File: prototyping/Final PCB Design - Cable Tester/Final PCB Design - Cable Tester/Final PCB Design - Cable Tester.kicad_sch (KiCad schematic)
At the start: 42 parts, among them J1 Massimo Connector, J2 Banana Jack, J3 Barrel Jack, J4 Conn_01x28_Socket, J5 Conn_01x28_Socket, J6 Touchscreen HMI, J7 Debug Connections, J8 SD Card Reader, J9 2908-05WB-MG, SW1 Rocker Switch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

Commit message: Update traces.
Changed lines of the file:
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@@
 (kicad_sch
-	(version 20231120)
+	(version 20250114)
 	(generator "eeschema")
-	(generator_version "8.0")
+	(generator_version "9.0")
 	(paper "A4")
+	(rectangle
+		(start 19.05 17.145)
+		(end 161.925 52.705)
+		(stroke
+			(width 0)
+			(type default)
+		)
+		(fill
+			(type none)
+		)
+	)
+	(text "Power"
+		(exclude_from_sim no)
+		(at 65.024 22.606 0)
+		(effects
+			(font
+				(size 2.032 2.032)
+				(thickness 0.4064)
+				(bold yes)
+			)
+		)
+	)
+	(text "Signal Relay"
+		(exclude_from_sim no)
+		(at 209.296 48.514 0)
+		(effects
+			(font
+				(size 2.032 2.032)
+				(thickness 0.4064)
+				(bold yes)
+			)
+		)
+	)
+	(text "AVR128DB48\nMicrocontroller"
+		(exclude_from_sim no)
+		(at 92.456 64.77 0)
+		(effects
+			(font
+				(size 2.54 2.54)
+				(thickness 0.508)
+				(bold yes)
+			)
+		)
+	)
+	(text "Analog IF"
+		(exclude_from_sim no)
+		(at 240.284 59.436 0)
+		(effects
+			(font
+				(size 2.032 2.032)
+				(thickness 0.4064)
+				(bold yes)
+			)
+		)
+	)
 	(junction
 		(at 269.24 110.49)
@@
 		)
 	)
-	(rectangle
-		(start 19.05 17.145)
-		(end 161.925 52.705)
-		(stroke
-			(width 0)
-			(type default)
-		)
-		(fill
-			(type none)
-		)
-	)
-	(text "Power"
-		(exclude_from_sim no)
-		(at 65.024 22.606 0)
-		(effects
-			(font
-				(size 2.032 2.032)
-				(thickness 0.4064)
-				(bold yes)
-			)
-		)
-	)
-	(text "Signal Relay"
-		(exclude_from_sim no)
-		(at 209.296 48.514 0)
-		(effects
-			(font
-				(size 2.032 2.032)
-				(thickness 0.4064)
-				(bold yes)
-			)
-		)
-	)
-	(text "AVR128DB48\nMicrocontroller"
-		(exclude_from_sim no)
-		(at 92.456 64.77 0)
-		(effects
-			(font
-				(size 2.54 2.54)
-				(thickness 0.508)
-				(bold yes)
-			)
-		)
-	)
-	(text "Analog IF"
-		(exclude_from_sim no)
-		(at 240.284 59.436 0)
-		(effects
-			(font
-				(size 2.032 2.032)
-				(thickness 0.4064)
-				(bold yes)
-			)
-		)
-	)
 	(label "9V"
 		(at 39.37 33.02 0)
@@
 		)
 	)
+	(embedded_fonts no)
 )

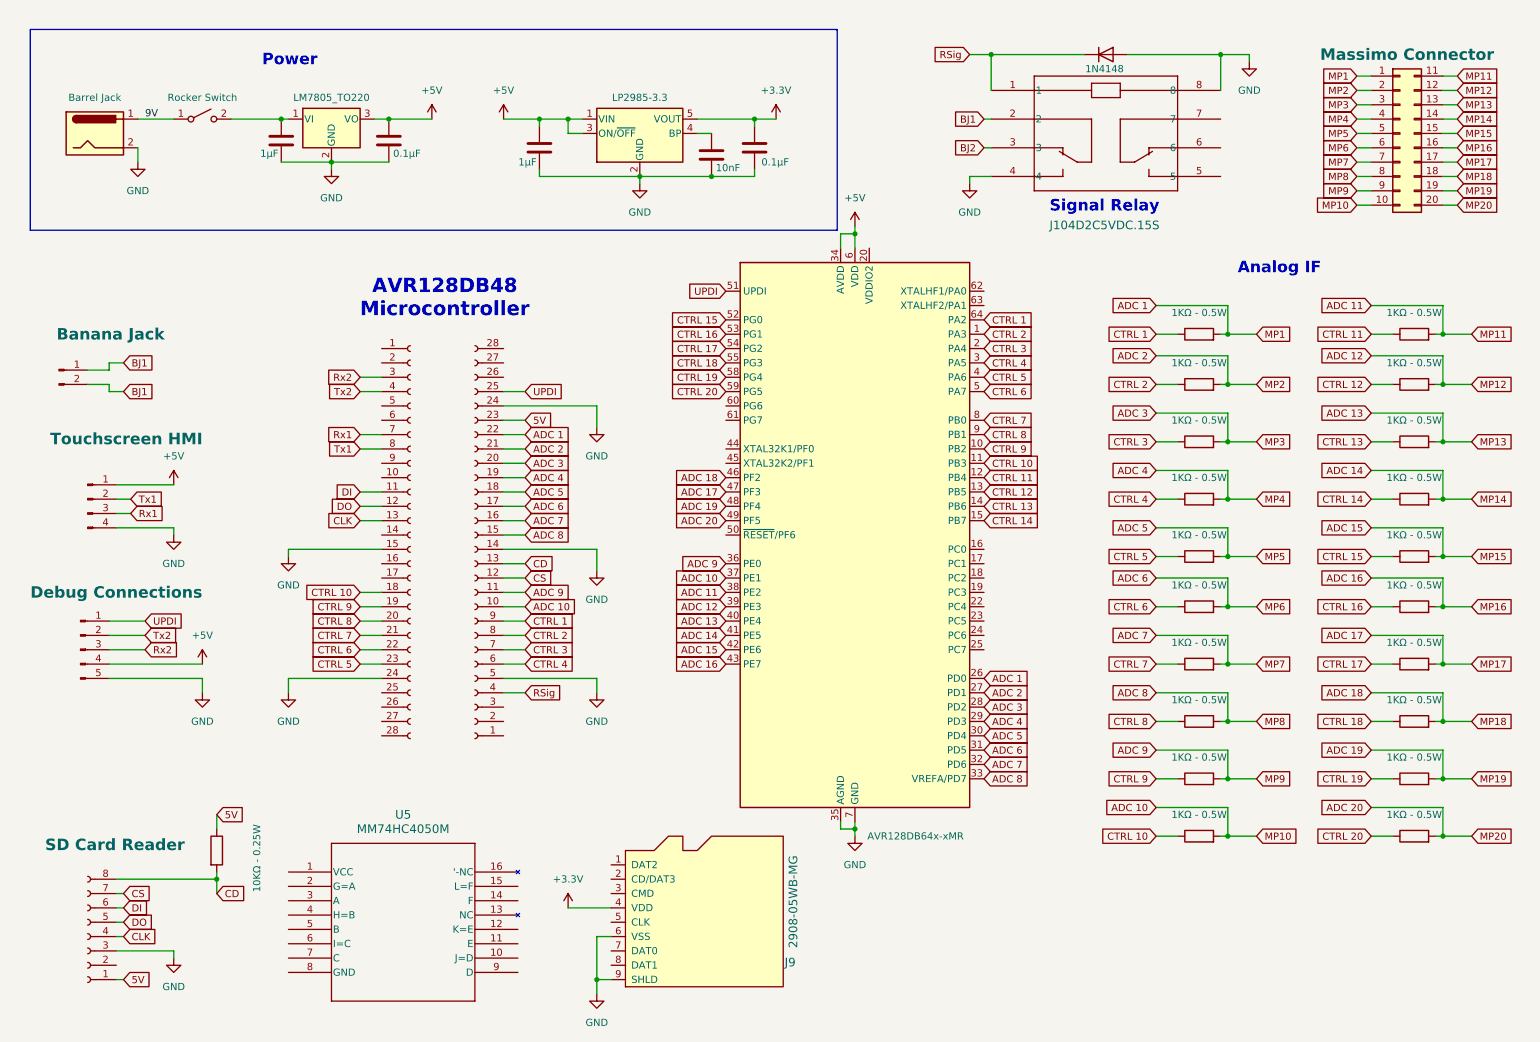
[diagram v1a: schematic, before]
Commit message: Final PCB Schematic updates
updated the pinout for the 64pin MCU, added the FT232RL for rs232 translation, added a micro USB to be the debug connection, added a single pin for UPDI connection.
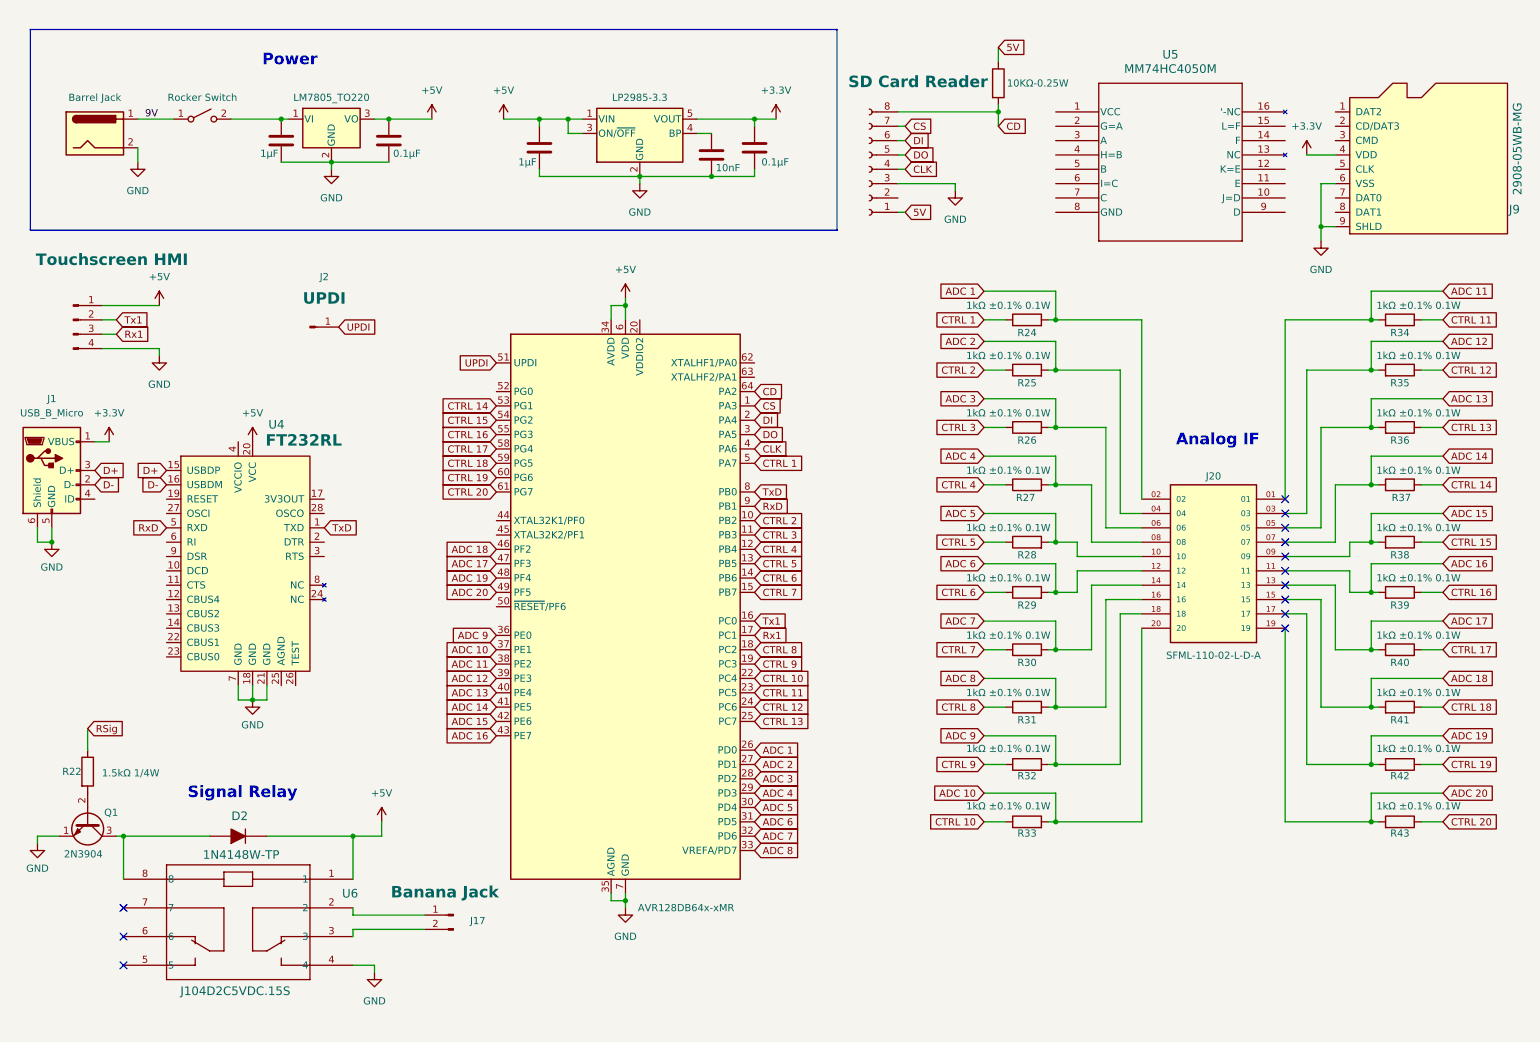
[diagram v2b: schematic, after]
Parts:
- removed D1: 1N4148, Diode_THT:D_DO-35_SOD27_P7.62mm_Horizontal, symbol Diode:1N4148
- removed J1: Massimo Connector, symbol Connector_Generic:Conn_02x10_Top_Bottom
- removed J2: Banana Jack, symbol Connector:Conn_01x02_Pin
- removed J4, J5: Conn_01x28_Socket, symbol Connector:Conn_01x28_Socket
- removed J7: Debug Connections, symbol Connector:Conn_01x05_Pin
- removed R10, R11, R12, R13, R14, R15, R16, R17, R18, R19, R2, R20, R21, R3, R4, R5, R6, R7, R8, R9: 1KΩ - 0.5W, symbol Device:R
- removed U4: J104D2C5VDC.15S, RELAY8_J104D2C5VDC.20S_CRS, symbol 2025-01-29_01-04-30:J104D2C5VDC.20S
- added D2: 1N4148W-TP, digikey-footprints:SOD-123, symbol dk_Diodes-Rectifiers-Single:1N4148W-TP
- added J1: USB_B_Micro, symbol Connector:USB_B_Micro
- added J17: Banana Jack, Connector_PinHeader_2.54mm:PinHeader_1x02_P2.54mm_Vertical, symbol Connector:Conn_01x02_Pin
- added J2: UPDI, Connector_PinHeader_1.00mm:PinHeader_1x01_P1.00mm_Vertical, symbol Connector:Conn_01x01_Pin
- added J20: SFML-110-02-L-D-A, KiCad Symbols and Footprints:SAMTEC_SFML-110-02-L-D-A, symbol SFML-110-02-L-D-A:SFML-110-02-L-D-A
- added Q1: 2N3904, Package_TO_SOT_THT:TO-92_Inline, symbol Transistor_BJT:2N3904
- added R22: 1.5kΩ 1/4W, KiCad Symbols and Footprints:RES_ERA8AEB152V, symbol Device:R
- added R24, R25, R26, R27, R28, R29, R30, R31, R32, R33, R34, R35, R36, R37, R38, R39, R40, R41, R42, R43: 1kΩ ±0.1% 0.1W, KiCad Symbols and Footprints:RES_0816_SUS, symbol Device:R
- added U4: FT232RL, digikey-footprints:SSOP-28_W5.30mm, symbol dk_Interface-Controllers:FT232RL-REEL
- added U6: J104D2C5VDC.15S, KiCad Symbols and Footprints:RELAY8_J104D2C5VDC.20S_CRS, symbol 2025-01-29_01-04-30:J104D2C5VDC.20S
- R1: value 10KΩ - 0.25W -> 10KΩ-0.25W
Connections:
- net +3.3V: now also J1.1 (VBUS)
- net +5V: now also D2.K, U4.20 (VCC), U6.1
- net ADC 1: now also J20.02, R24.2
- net ADC 10: now also J20.20, R33.2
- net ADC 11: now also J20.01, R34.2
- net ADC 12: now also J20.03, R35.2
- net ADC 13: now also J20.05, R36.2
- net ADC 14: now also J20.07, R37.2
- net ADC 15: now also J20.09, R38.2
- net ADC 16: now also J20.11, R39.2
- net ADC 17: now also J20.13, R40.2
- net ADC 18: now also J20.15, R41.2
- net ADC 19: now also J20.17, R42.2
- net ADC 2: now also J20.04, R25.2
- net ADC 20: now also J20.19, R43.2
- net ADC 3: now also J20.06, R26.2
- net ADC 4: now also J20.08, R27.2
- net ADC 5: now also J20.10, R28.2
- net ADC 6: now also J20.12, R29.2
- net ADC 7: now also J20.14, R30.2
- net ADC 8: now also J20.16, R31.2
- net ADC 9: now also J20.18, R32.2
- net CD: now also U1.64 (PA2)
- net CLK: now also U1.4 (PA6)
- net CS: now also U1.1 (PA3)
- net CTRL 1: now also U1.5 (PA7), R24.1; no longer U1.64 (PA2)
- net CTRL 10: now also U1.22 (PC4), R33.1; no longer U1.11 (PB3)
- net CTRL 11: now also U1.23 (PC5), R34.1; no longer U1.12 (PB4)
- net CTRL 12: now also U1.24 (PC6), R35.1; no longer U1.13 (PB5)
- net CTRL 13: now also U1.25 (PC7), R36.1; no longer U1.14 (PB6)
- net CTRL 14: now also U1.53 (PG1), R37.1; no longer U1.15 (PB7)
- net CTRL 15: now also U1.54 (PG2), R38.1; no longer U1.52 (PG0)
- net CTRL 16: now also U1.55 (PG3), R39.1; no longer U1.53 (PG1)
- net CTRL 17: now also U1.58 (PG4), R40.1; no longer U1.54 (PG2)
- net CTRL 18: now also U1.59 (PG5), R41.1; no longer U1.55 (PG3)
- net CTRL 19: now also U1.60 (PG6), R42.1; no longer U1.58 (PG4)
- net CTRL 2: now also U1.10 (PB2), R25.1; no longer U1.1 (PA3)
- net CTRL 20: now also U1.61 (PG7), R43.1; no longer U1.59 (PG5)
- net CTRL 3: now also U1.11 (PB3), R26.1; no longer U1.2 (PA4)
- net CTRL 4: now also U1.12 (PB4), R27.1; no longer U1.3 (PA5)
- net CTRL 5: now also U1.13 (PB5), R28.1; no longer U1.4 (PA6)
- net CTRL 6: now also U1.14 (PB6), R29.1; no longer U1.5 (PA7)
- net CTRL 7: now also U1.15 (PB7), R30.1; no longer U1.8 (PB0)
- net CTRL 8: now also U1.18 (PC2), R31.1; no longer U1.9 (PB1)
- net CTRL 9: now also U1.19 (PC3), R32.1; no longer U1.10 (PB2)
- net DI: now also U1.2 (PA4)
- net DO: now also U1.3 (PA5)
- net GND: now also J1.5 (GND), J1.6 (Shield), Q1.1 (E), U4.18 (GND), U4.21 (GND), U4.7 (GND), U6.4
- net RSig: now also R22.1
- net Rx1: now also U1.17 (PC1)
- net Tx1: now also U1.16 (PC0)
- net UPDI: now also J2.1 (Pin_1)
- new net: J17.1 (Pin_1), U6.2
- new net: J17.2 (Pin_2), U6.3
- new net: Q1.2 (B), R22.2
- new net: D2.A, Q1.3 (C), U6.8
- new net D+: J1.3 (D+), U4.15 (USBDP)
- new net D-: J1.2 (D-), U4.16 (USBDM)
- new net RxD: U1.9 (PB1), U4.5 (RXD)
- new net TxD: U1.8 (PB0), U4.1 (TXD)
- no-connect marks 0 -> 13
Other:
- note removed: "AVR128DB48 Microcontroller"
- moved on the sheet: J9, U5

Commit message: Final PCB schematic update
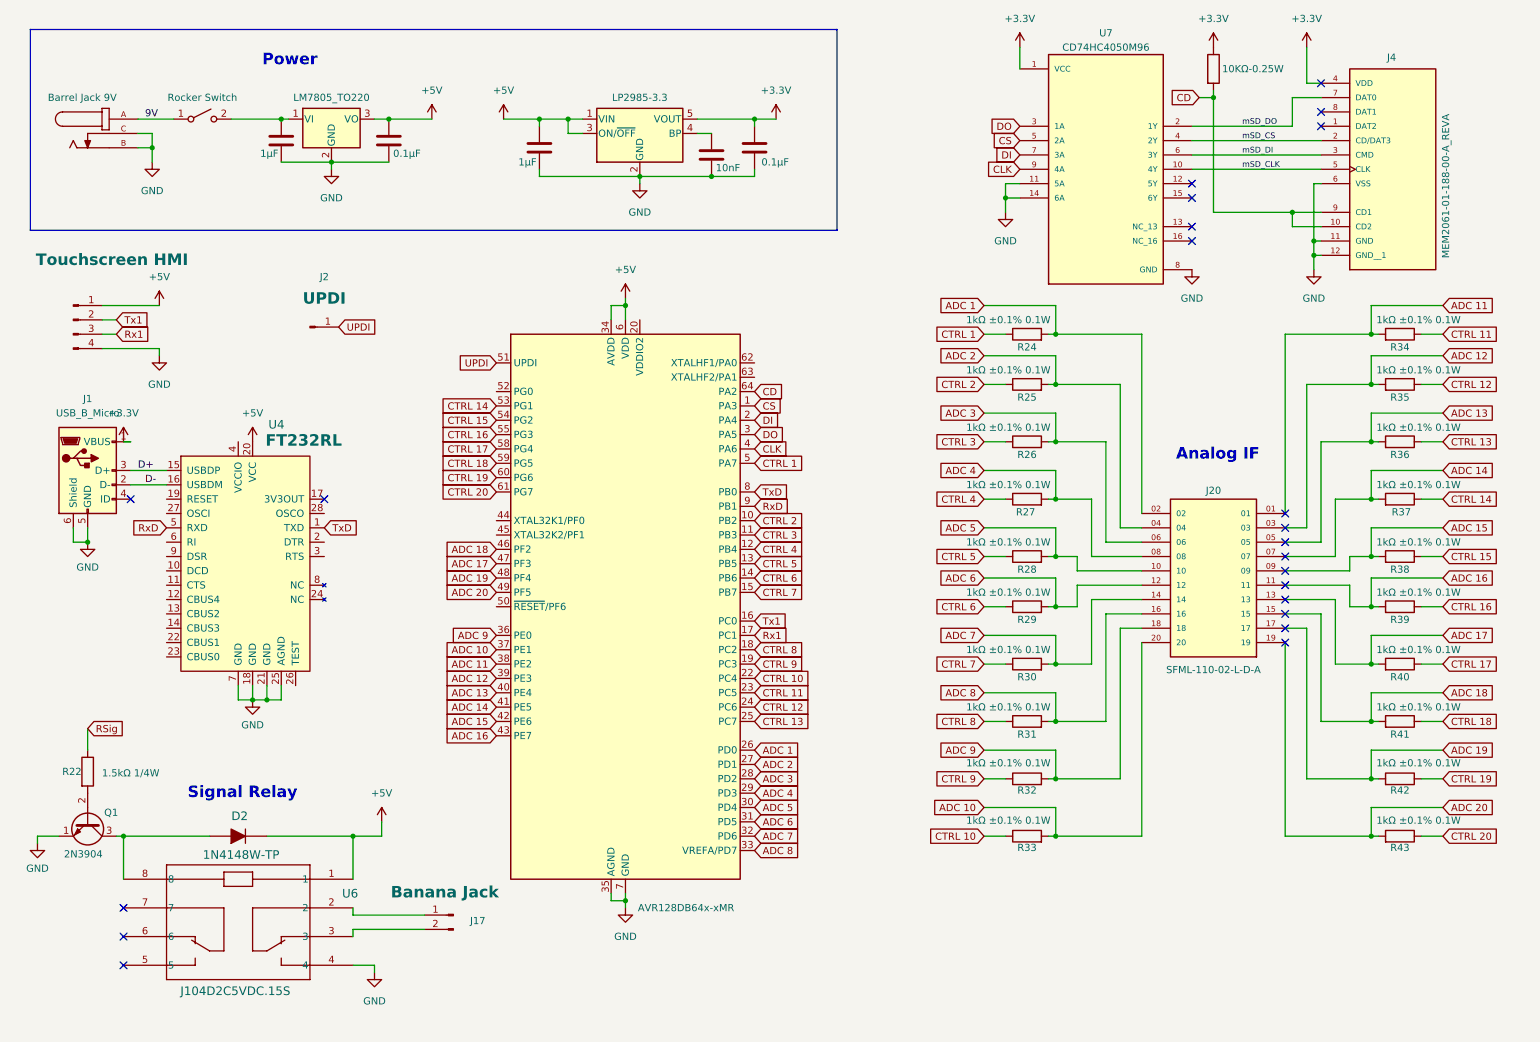
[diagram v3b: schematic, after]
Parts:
- removed J3: Barrel Jack, symbol Connector:Barrel_Jack
- removed J8: SD Card Reader, symbol Connector:Conn_01x08_Socket
- removed J9: 2908-05WB-MG, digikey-footprints:MicroSD_2908-05WB-MG, symbol dk_Memory-Connectors-PC-Card-Sockets:2908-05WB-MG
- removed R1: 10KΩ-0.25W, symbol Device:R
- removed U5: MM74HC4050M, SOIC16_3P988X10_ONS, symbol 2025-03-04_01-10-27:MM74HC4050M
- added J4: MEM2061-01-188-00-A_REVA, KiCad Symbols and Footprints:GCT_MEM2061-01-188-00-A_REVA, symbol MEM2061-01-188-00-A_REVA:MEM2061-01-188-00-A_REVA
- added J5: Barrel Jack 9V, KiCad Symbols and Footprints:TENSILITY_54-00129, symbol 54-00129:54-00129
- added R2: 10KΩ-0.25W, KiCad Symbols and Footprints:RC0402N_PAN, symbol Device:R
- added U7: CD74HC4050M96, CD74HC4050M96:SOIC127P600X175-16N, symbol CD74HC4050M96:CD74HC4050M96
- C1, C3: footprint (none) -> KiCad Symbols and Footprints:CAP_CL10_SAM
- C2, C4: footprint (none) -> KiCad Symbols and Footprints:CAP_CL05_SAM
- C5: footprint (none) -> KiCad Symbols and Footprints:CAPC10555_55N_KEM
- J1: footprint (none) -> Connector_USB:USB_Micro-AB_Molex_47590-0001
- J2: footprint Connector_PinHeader_1.00mm:PinHeader_1x01_P1.00mm_Vertical -> Connector_PinHeader_2.54mm:PinHeader_1x01_P2.54mm_Vertical
- J6: footprint (none) -> Connector_PinHeader_2.54mm:PinHeader_1x04_P2.54mm_Vertical
- SW1: footprint (none) -> Connector_PinHeader_1.00mm:PinHeader_1x02_P1.00mm_Vertical
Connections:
- net +3.3V: now also J4.4 (VDD), R2.1, U7.1 (VCC)
- net 9V: now also J5.A
- net CD: now also J4.10 (CD2), J4.9 (CD1), R2.2
- net CLK: now also U7.9 (4A)
- net CS: now also U7.5 (2A)
- net DI: now also U7.7 (3A)
- net DO: now also U7.3 (1A)
- net GND: now also U4.25 (AGND), J4.11 (GND), J4.12 (GND__1), J4.6 (VSS), J5.B, J5.C, U7.11 (5A), U7.14 (6A), U7.8 (GND)
- new net mSD_CLK: J4.5 (CLK), U7.10 (4Y)
- new net mSD_CS: J4.2 (CD/DAT3), U7.4 (2Y)
- new net mSD_DI: J4.3 (CMD), U7.6 (3Y)
- new net mSD_DO: J4.7 (DAT0), U7.2 (1Y)
- no-connect marks 13 -> 22
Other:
- moved on the sheet: J1, J20, R24, R25, R26, R27, R28, R29, R30, R31, R32, R33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

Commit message: Final PCB Schematic and PCB layout update
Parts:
- removed J1: USB_B_Micro, Connector_USB:USB_Micro-AB_Molex_47590-0001, symbol Connector:USB_B_Micro
- removed J2: UPDI, Connector_PinHeader_2.54mm:PinHeader_1x01_P2.54mm_Vertical, symbol Connector:Conn_01x01_Pin
- removed U4: FT232RL, digikey-footprints:SSOP-28_W5.30mm, symbol dk_Interface-Controllers:FT232RL-REEL
- added J3: Debug Connection, Connector_PinHeader_2.54mm:PinHeader_1x05_P2.54mm_Vertical, symbol Connector:Conn_01x05_Pin
- SW1: footprint Connector_PinHeader_1.00mm:PinHeader_1x02_P1.00mm_Vertical -> Connector_PinHeader_2.54mm:PinHeader_1x02_P2.54mm_Vertical
- U7: footprint CD74HC4050M96:SOIC127P600X175-16N -> KiCad Symbols and Footprints:SOIC127P600X175-16N
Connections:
- net CD is gone; now on net GND: J4.10 (CD2), J4.9 (CD1), R2.2, U1.64 (PA2)
- net mSD_CLK is gone; now on net GND: J4.5 (CLK), U7.10 (4Y)
- net mSD_CS is gone; now on net GND: J4.2 (CD/DAT3), U7.4 (2Y)
- net mSD_DI is gone; now on net GND: J4.3 (CMD), U7.6 (3Y)
- net mSD_DO is gone; now on net GND: J4.7 (DAT0), U7.2 (1Y)
- net +5V: now also J3.2 (Pin_2)
- net ADC 17: now also U1.46 (PF2); no longer U1.47 (PF3)
- net ADC 18: now also U1.47 (PF3); no longer U1.46 (PF2)
- net GND: now also J3.1 (Pin_1)
- net RSig: now also U1.52 (PG0)
- net RxD: now also J3.4 (Pin_4)
- net TxD: now also J3.3 (Pin_3)
- net UPDI: now also J3.5 (Pin_5)
- no-connect marks 22 -> 20
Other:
- moved on the sheet: D2, J17, J20, J4, Q1, R22, R24, R25, R26, R27, R28, R29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
